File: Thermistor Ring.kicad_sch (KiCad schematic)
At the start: 20 parts, among them IC1 MAX30210ENL+, IC2 MAX30210ENL+, IC3 MAX30210ENL+, IC4 MAX30210ENL+, IC5 MAX30210ENL+, IC6 MAX30210ENL+, J1 Conn_01x04_Socket, J3 Conn_01x03_Socket, U1 TPS7A2018PDBVR

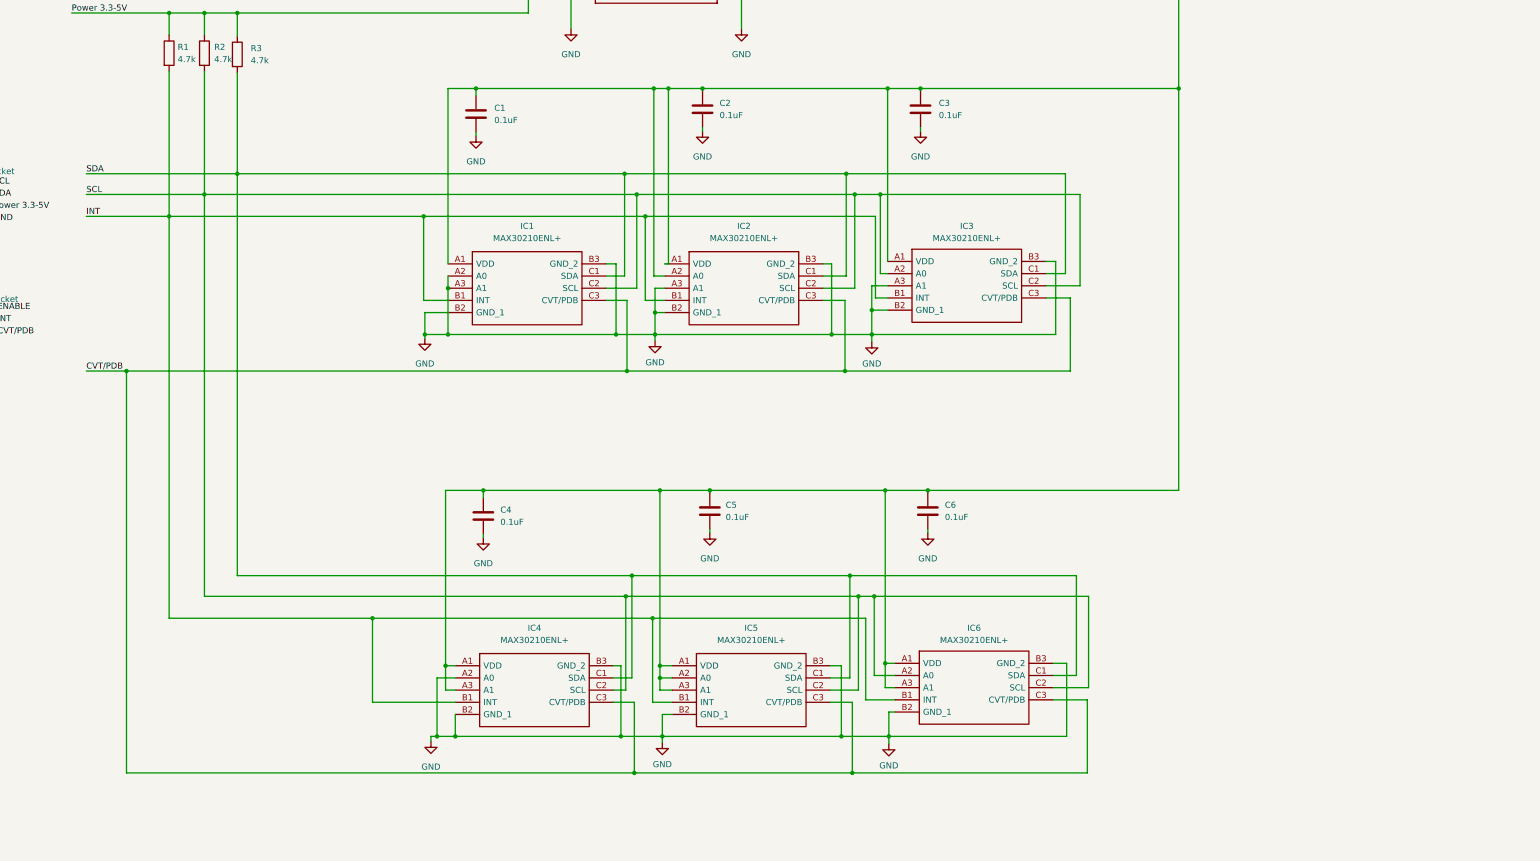
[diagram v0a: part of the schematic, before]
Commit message: schematic updated for MCP9808 temperature sensor
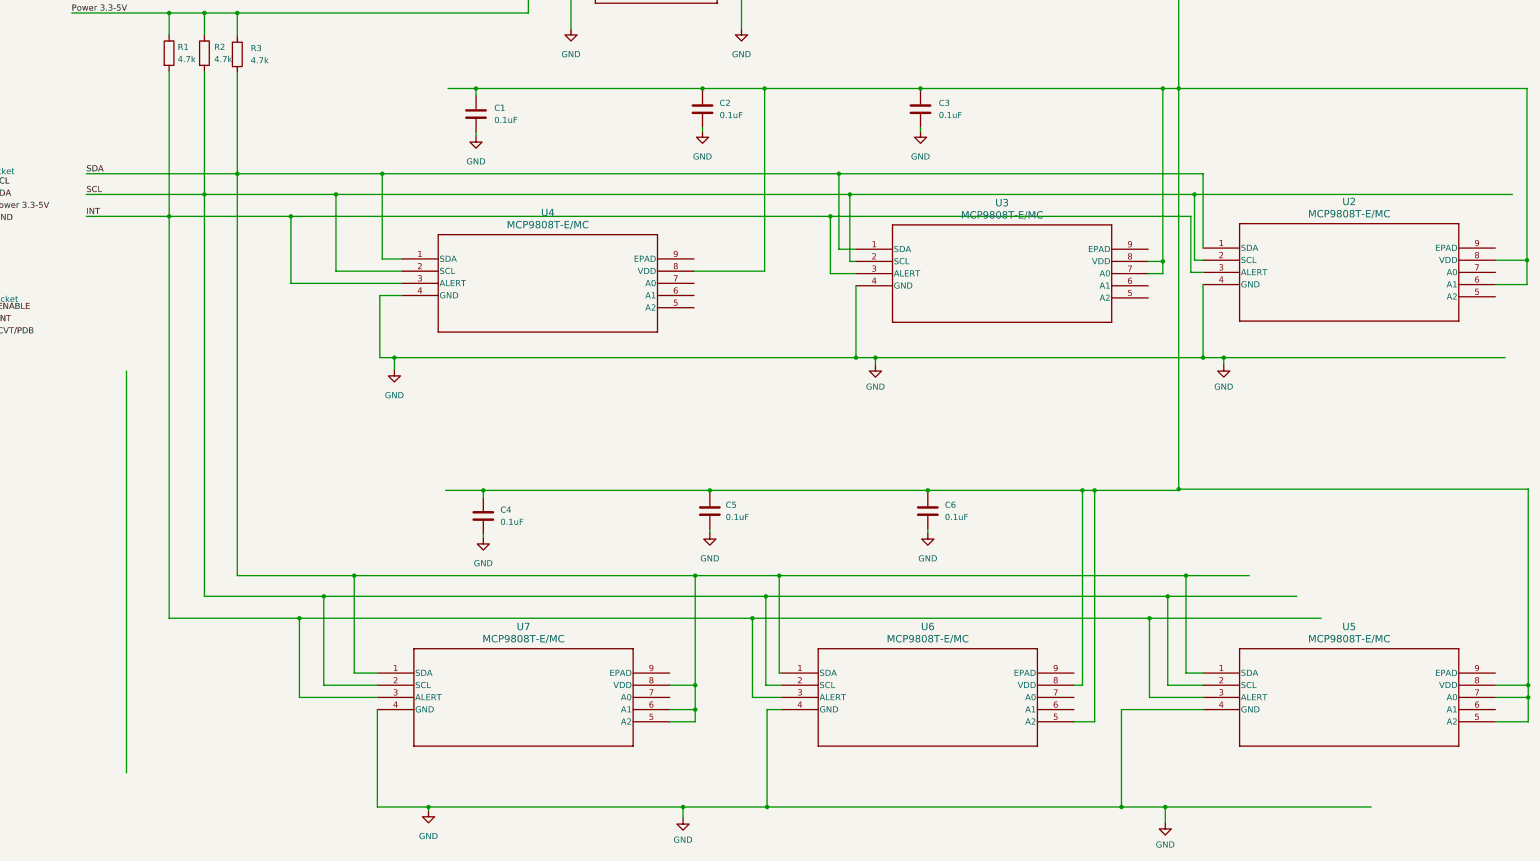
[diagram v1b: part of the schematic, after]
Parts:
- removed IC1, IC2, IC3, IC4, IC5, IC6: MAX30210ENL+, MAX30210:21-100600_N90A0&plus_1_ADI, symbol MAX30210:MAX30210ENL+
- added U2, U3, U4, U5, U6, U7: MCP9808T-E/MC, DFN8_2x3MC_MCH, symbol mcp9808:MCP9808T-E_MC
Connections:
- net GND: now also U2.4 (GND), U3.4 (GND), U4.4 (GND), U5.4 (GND), U6.4 (GND), U7.4 (GND)
- net INT: now also U2.3 (ALERT), U3.3 (ALERT), U4.3 (ALERT), U5.3 (ALERT), U6.3 (ALERT), U7.3 (ALERT)
- net SCL: now also U2.2 (SCL), U3.2 (SCL), U4.2 (SCL), U5.2 (SCL), U6.2 (SCL), U7.2 (SCL)
- net SDA: now also U2.1 (SDA), U3.1 (SDA), U4.1 (SDA), U5.1 (SDA), U6.1 (SDA), U7.1 (SDA), U7.5 (A2), U7.6 (A1), U7.8 (VDD)
- net VDD: now also U2.6 (A1), U2.8 (VDD), U3.7 (A0), U3.8 (VDD), U4.8 (VDD), U5.5 (A2), U5.7 (A0), U5.8 (VDD), U6.5 (A2), U6.8 (VDD)

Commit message: shrinking ring
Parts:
- removed J3: Conn_01x03_Socket, Connector_JST:JST_XH_B3B-XH-A_1x03_P2.50mm_Vertical, symbol Connector:Conn_01x03_Socket
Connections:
- net GND: now also U4.9 (EPAD)
- net Power 3.3-5V: now also C1.1, C2.1, C3.1, C4.1, C6.1, C8.1, U1.5 (OUT), U2.6 (A1), U2.8 (VDD), U3.7 (A0), U3.8 (VDD), U4.8 (VDD), U5.5 (A2), U5.7 (A0), U5.8 (VDD), U6.5 (A2), U6.8 (VDD)
- removed net VDD: C1.1, C2.1, C3.1, C4.1, C5.1, C6.1, C8.1, U1.5 (OUT), U2.6 (A1), U2.8 (VDD), U3.7 (A0), U3.8 (VDD), U4.8 (VDD), U5.5 (A2), U5.7 (A0), U5.8 (VDD), U6.5 (A2), U6.8 (VDD)

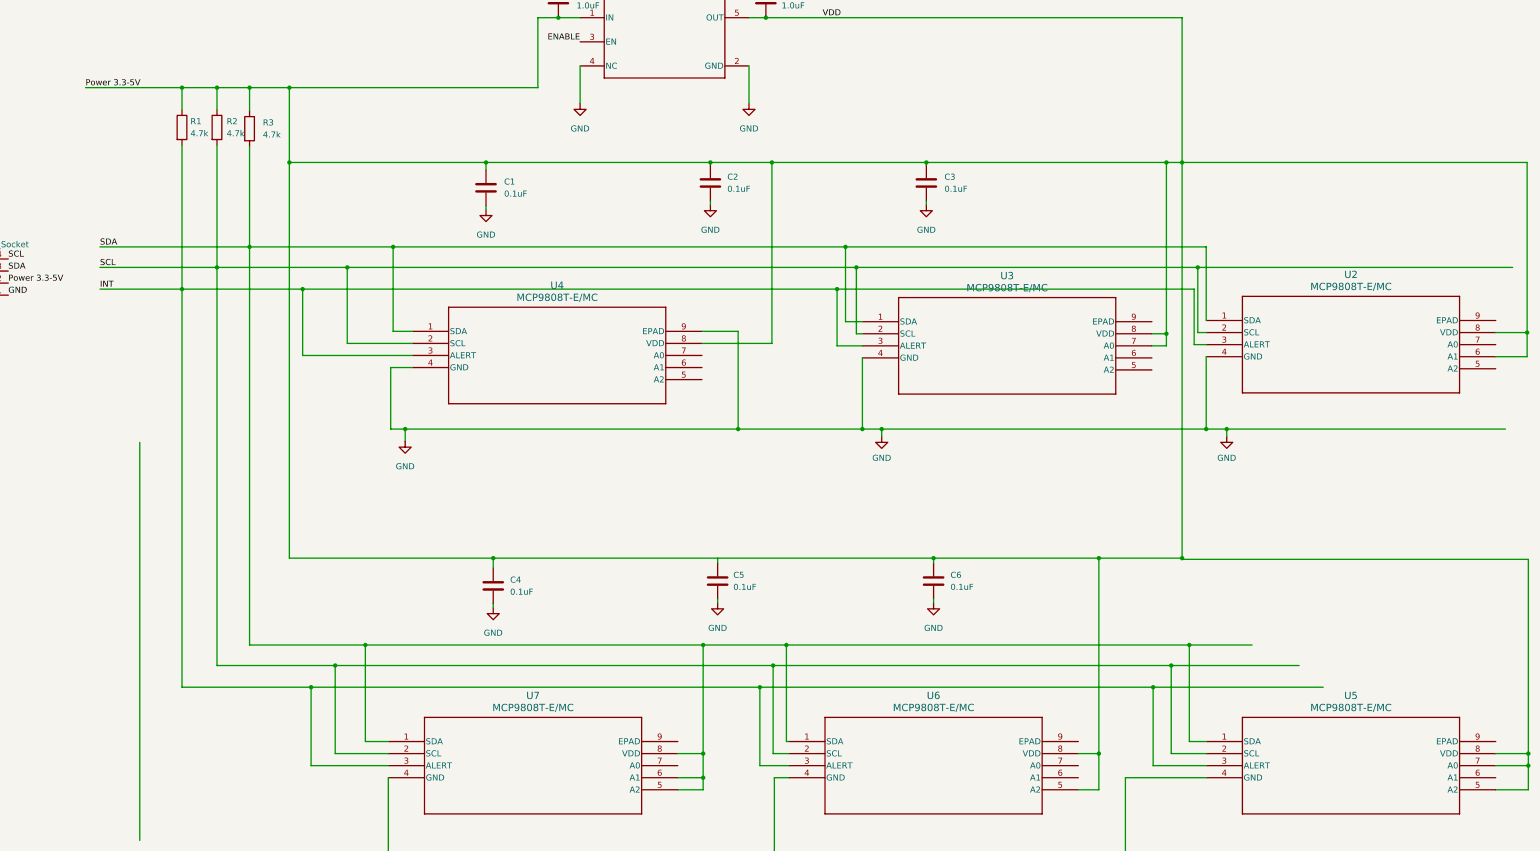
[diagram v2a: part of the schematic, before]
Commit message: smaller ring first draft
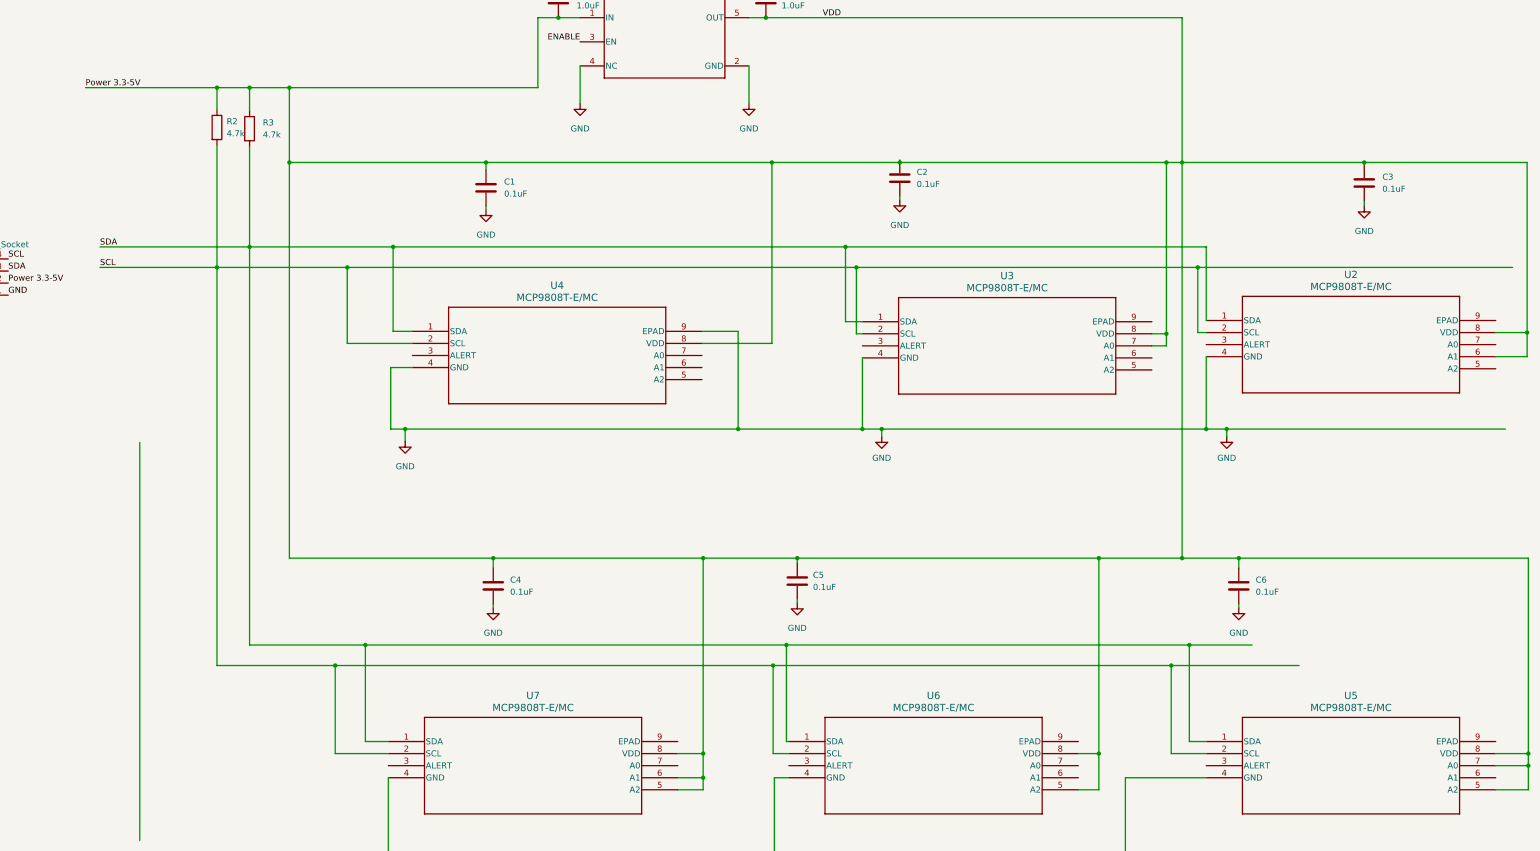
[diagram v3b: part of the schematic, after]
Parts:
- removed R1: 4.7k, Resistor_SMD:R_0805_2012Metric, symbol Device:R
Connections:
- net Power 3.3-5V: now also C5.1, U7.5 (A2), U7.6 (A1), U7.8 (VDD)
- net SDA: no longer U7.5 (A2), U7.6 (A1), U7.8 (VDD)
- removed net INT: U2.3 (ALERT), U3.3 (ALERT), U4.3 (ALERT), U5.3 (ALERT), U6.3 (ALERT), U7.3 (ALERT)
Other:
- moved on the sheet: C2, C3, C5, C6

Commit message: wip: some fixes
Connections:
- net GND: now also U2.5 (A2), U2.7 (A0), U2.9 (EPAD)
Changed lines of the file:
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@@
     (effects (font (size 1.27 1.27)) (justify left bottom))
+  )
+  (symbol (lib_id "power:GND") (at 293.878 56.642 90) (unit 1)
+    (in_bom yes) (on_board yes) (dnp no) (fields_autoplaced)
+    (property "Reference" "#PWR018" (at 300.228 56.642 0)
+      (effects (font (size 1.27 1.27)) hide)
+    )
+    (property "Value" "GND" (at 297.18 56.642 90)
+      (effects (font (size 1.27 1.27)) (justify right))
+    )
+    (property "Footprint" "" (at 293.878 56.642 0)
+      (effects (font (size 1.27 1.27)) hide)
+    )
+    (property "Datasheet" "" (at 293.878 56.642 0)
+      (effects (font (size 1.27 1.27)) hide)
+    )
+    (pin "1")
+    (instances
+      (project "Thermistor Ring"
+        (path "/6637e588-6cff-41c7-8818-9eea1dd986d9"
+          (reference "#PWR018") (unit 1)
+        )
+      )
+    )
   )
   (symbol (lib_id "Device:C") (at 140.208 -16.002 180) (unit 1)
@@
         (path "/6637e588-6cff-41c7-8818-9eea1dd986d9"
           (reference "C2") (unit 1)
+        )
+      )
+    )
+  )
+  (symbol (lib_id "power:GND") (at 293.878 51.562 90) (unit 1)
+    (in_bom yes) (on_board yes) (dnp no) (fields_autoplaced)
+    (property "Reference" "#PWR019" (at 300.228 51.562 0)
+      (effects (font (size 1.27 1.27)) hide)
+    )
+    (property "Value" "GND" (at 297.6074 51.562 90)
+      (effects (font (size 1.27 1.27)) (justify right))
+    )
+    (property "Footprint" "" (at 293.878 51.562 0)
+      (effects (font (size 1.27 1.27)) hide)
+    )
+    (property "Datasheet" "" (at 293.878 51.562 0)
+      (effects (font (size 1.27 1.27)) hide)
+    )
+    (pin "1")
+    (instances
+      (project "Thermistor Ring"
+        (path "/6637e588-6cff-41c7-8818-9eea1dd986d9"
+          (reference "#PWR019") (unit 1)
         )
       )
@@
         )
       )
+    )
+  )
+  (symbol (lib_id "power:GND") (at 293.878 61.722 90) (unit 1)
+    (in_bom yes) (on_board yes) (dnp no) (fields_autoplaced)
+    (property "Reference" "#PWR017" (at 300.228 61.722 0)
+      (effects (font (size 1.27 1.27)) hide)
+    )
+    (property "Value" "GND" (at 297.18 61.722 90)
+      (effects (font (size 1.27 1.27)) (justify right))
+    )
+    (property "Footprint" "" (at 293.878 61.722 0)
+      (effects (font (size 1.27 1.27)) hide)
+    )
+    (property "Datasheet" "" (at 293.878 61.722 0)
+      (effects (font (size 1.27 1.27)) hide)
+    )
+    (pin "1")
+    (instances
+      (project "Thermistor Ring"
+        (path "/6637e588-6cff-41c7-8818-9eea1dd986d9"
+          (reference "#PWR017") (unit 1)
+        )
+      )

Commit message: Update PCB and resolve DRC
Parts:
- U1: footprint TPS7A201:DBV0005A-IPC_A -> TPS7A2018PDBVR:DBV0005A-IPC_A
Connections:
- net GND: now also U2.3 (ALERT), U3.3 (ALERT), U3.5 (A2), U3.6 (A1), U3.9 (EPAD), U4.3 (ALERT), U4.5 (A2), U4.6 (A1), U4.7 (A0), U5.3 (ALERT), U5.6 (A1), U5.9 (EPAD), U6.3 (ALERT), U6.6 (A1), U6.7 (A0), U6.9 (EPAD), U7.3 (ALERT), U7.7 (A0), U7.9 (EPAD)
- net Power 3.3-5V: no longer C1.1, C2.1, C3.1, C4.1, C5.1, C6.1, C8.1, U1.5 (OUT), U2.6 (A1), U2.8 (VDD), U3.7 (A0), U3.8 (VDD), U4.8 (VDD), U5.5 (A2), U5.7 (A0), U5.8 (VDD), U6.5 (A2), U6.8 (VDD), U7.5 (A2), U7.6 (A1), U7.8 (VDD)
- new net VDD: C1.1, C2.1, C3.1, C4.1, C5.1, C6.1, C8.1, U1.5 (OUT), U2.6 (A1), U2.8 (VDD), U3.7 (A0), U3.8 (VDD), U4.8 (VDD), U5.5 (A2), U5.7 (A0), U5.8 (VDD), U6.5 (A2), U6.8 (VDD), U7.5 (A2), U7.6 (A1), U7.8 (VDD)
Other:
- moved on the sheet: C1, C2, C3, C4, C5, C6, C7, C8, J1, R2, R3, U1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
